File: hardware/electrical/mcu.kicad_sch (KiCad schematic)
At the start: 40 parts, among them J2 TC2030, Q8 2N7002, SW1 TS-1187A-B-A-B, SW2 EVQP7C01K, U8 STM32F446VET6, Y1 24MHz, Y2 32.768kHz

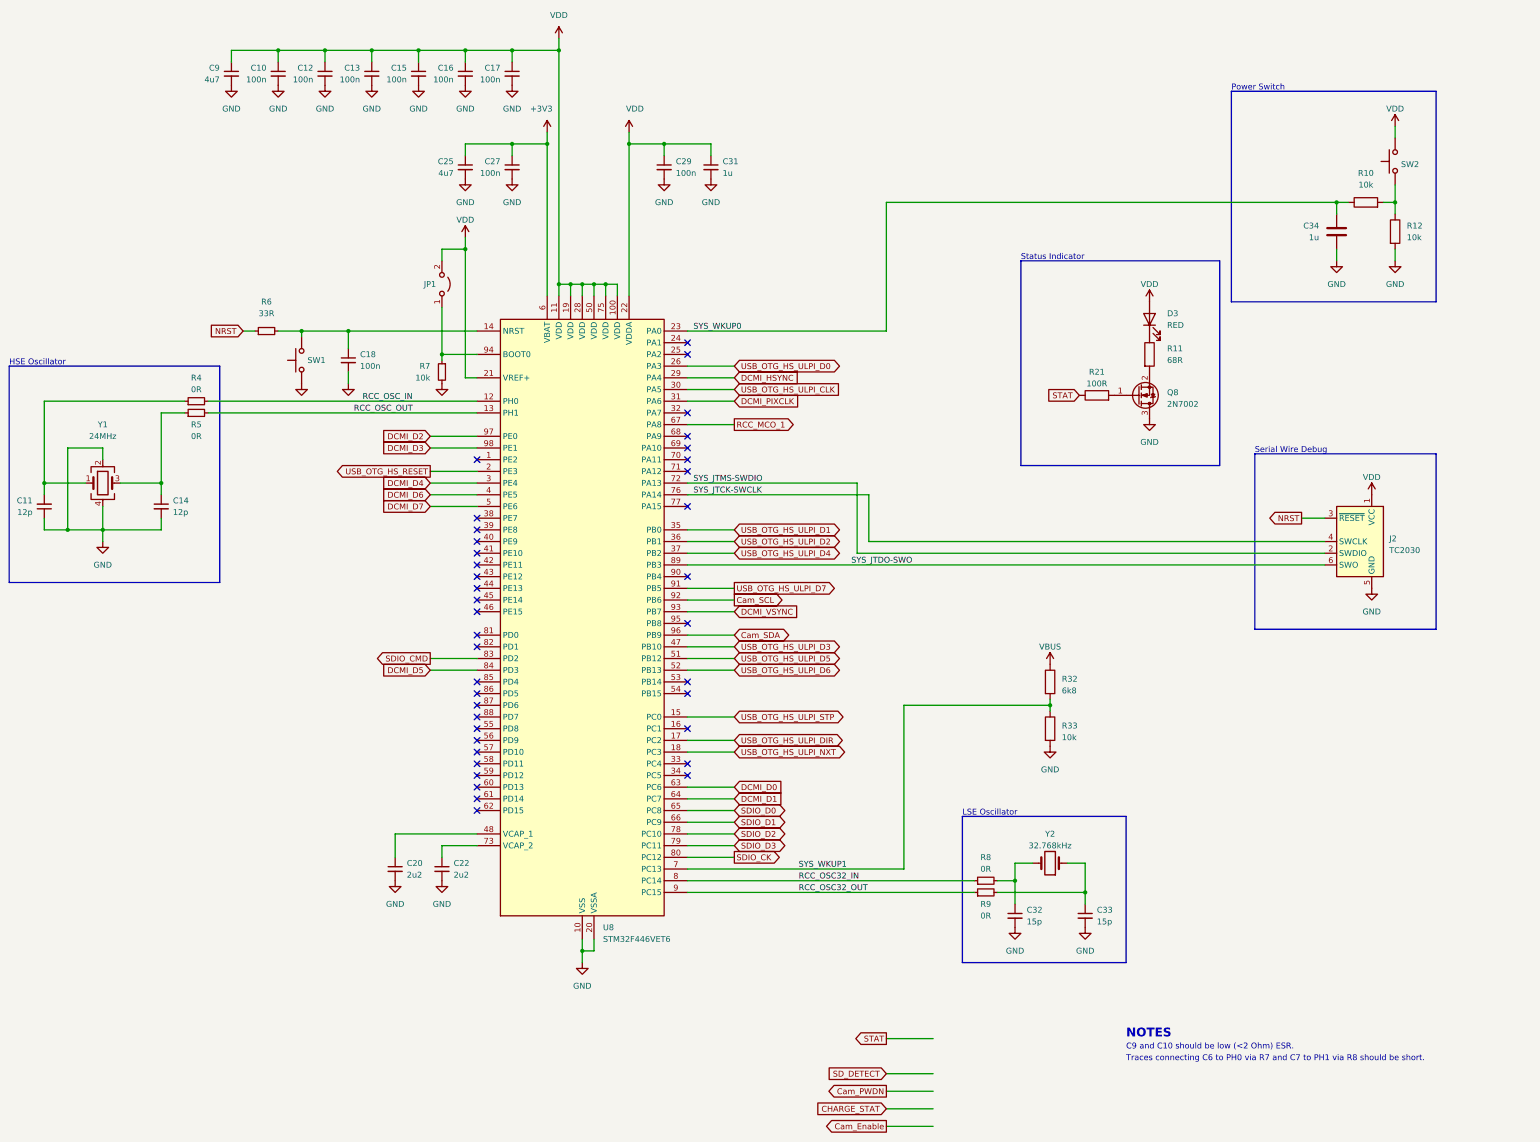
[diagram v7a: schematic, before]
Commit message: Revise power supply
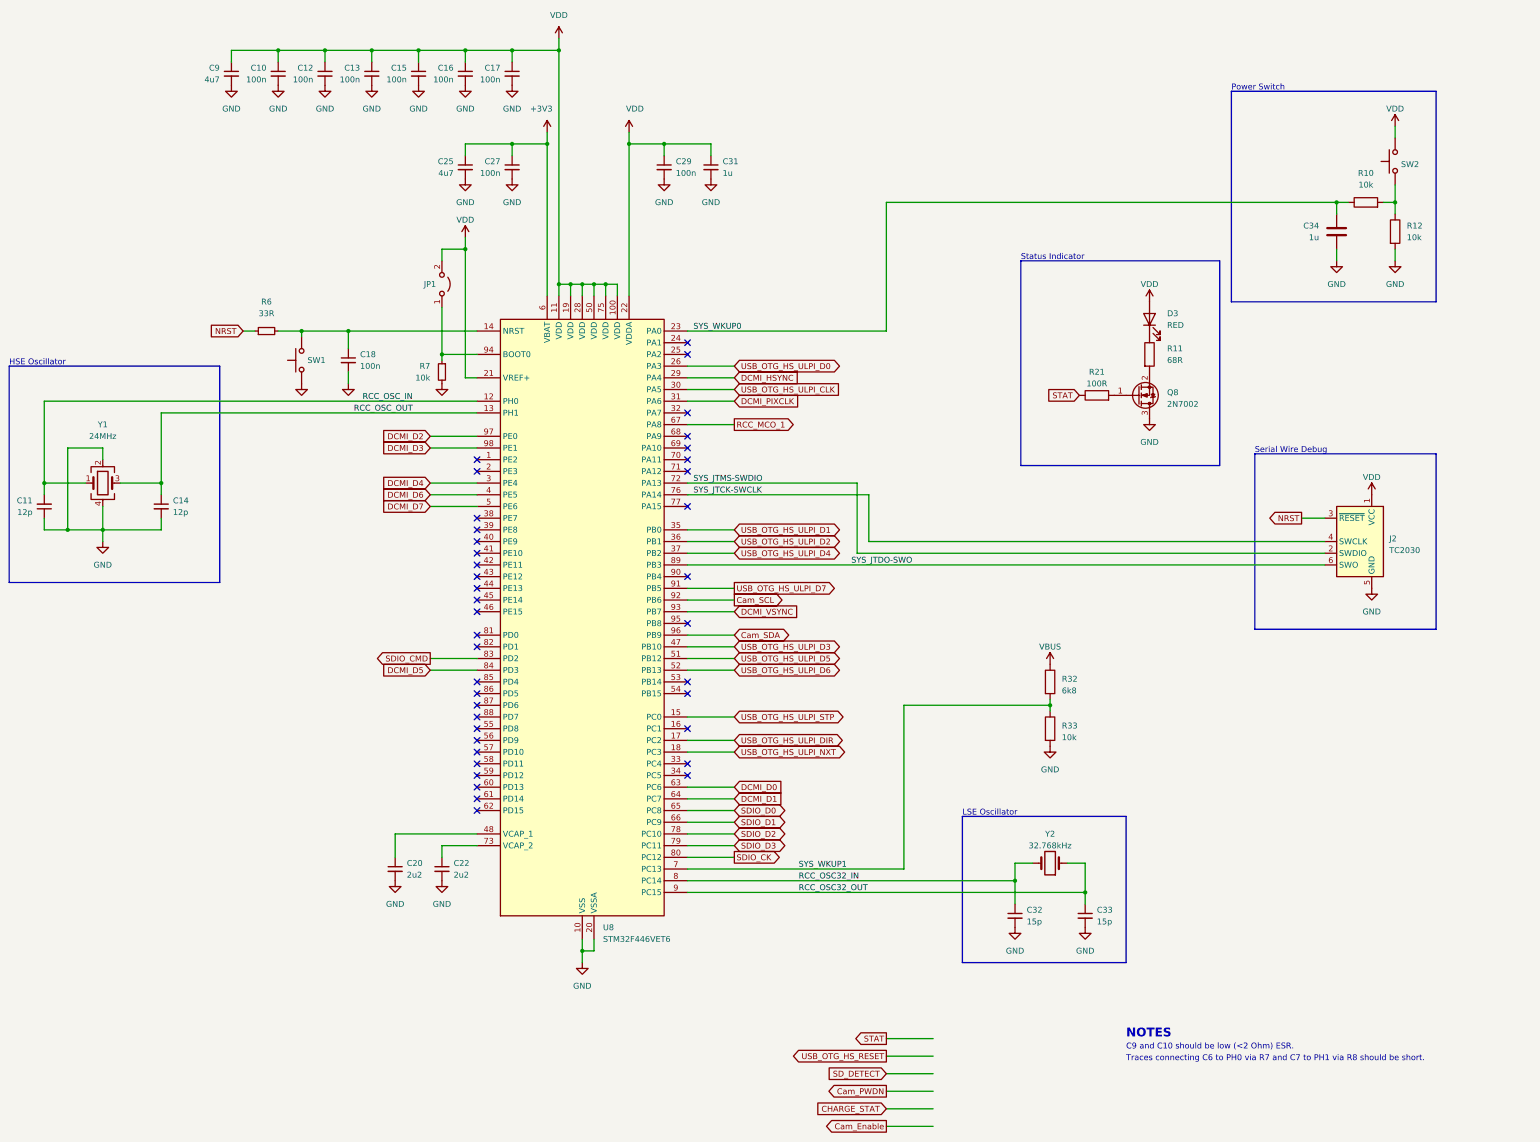
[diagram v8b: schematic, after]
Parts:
- removed R4, R5, R8, R9: 0R, Resistor_SMD:R_0603_1608Metric_Pad0.98x0.95mm_HandSolder, symbol Device:R_Small
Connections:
- net RCC_OSC32_IN: now also C32.1, Y2.2
- net RCC_OSC32_OUT: now also C33.1, Y2.1
- net RCC_OSC_IN: now also C11.2, Y1.1
- net RCC_OSC_OUT: now also C14.1, Y1.3
- net USB_OTG_HS_RESET: no longer U8.2 (PE3)
- no-connect marks 39 -> 40
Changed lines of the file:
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@@
   (no_connect (at 204.47 180.34))
   (no_connect (at 204.47 170.18))
+  (no_connect (at 158.75 124.46))
   (no_connect (at 158.75 182.88))
   (no_connect (at 158.75 121.92))
@@
     (stroke (width 0) (type default))
   )
-  (wire (pts (xy 158.75 124.46) (xy 148.59 124.46))
+  (wire (pts (xy 257.81 251.46) (xy 247.65 251.46))
     (stroke (width 0) (type default))
   )
@@
     (stroke (width 0) (type default))
   )
-  (wire (pts (xy 100.33 111.76) (xy 158.75 111.76))
+  (wire (pts (xy 90.17 111.76) (xy 158.75 111.76))
     (stroke (width 0) (type default))
   )
@@
     (stroke (width 0) (type default))
   )
-  (wire (pts (xy 90.17 111.76) (xy 95.25 111.76))
-    (stroke (width 0) (type default))
-  )
   (wire (pts (xy 135.89 33.02) (xy 135.89 35.56))
     (stroke (width 0) (type default))
@@
     (stroke (width 0) (type default))
   )
-  (wire (pts (xy 204.47 215.9) (xy 266.7 215.9))
-    (stroke (width 0) (type default))
-  )
   (wire (pts (xy 151.13 78.74) (xy 151.13 76.2))
     (stroke (width 0) (type default))
@@
     (stroke (width 0) (type default))
   )
-  (wire (pts (xy 290.83 215.9) (xy 271.78 215.9))
+  (wire (pts (xy 204.47 215.9) (xy 290.83 215.9))
     (stroke (width 0) (type default))
   )
@@
     (stroke (width 0) (type default))
   )
-  (wire (pts (xy 204.47 213.36) (xy 266.7 213.36))
-    (stroke (width 0) (type default))
-  )
   (wire (pts (xy 176.53 83.82) (xy 179.07 83.82))
     (stroke (width 0) (type default))
@@
     (stroke (width 0) (type default))
   )
-  (wire (pts (xy 271.78 213.36) (xy 275.59 213.36))
+  (wire (pts (xy 204.47 213.36) (xy 275.59 213.36))
     (stroke (width 0) (type default))
   )
@@
     (stroke (width 0) (type default))
   )
-  (wire (pts (xy 64.77 109.22) (xy 95.25 109.22))
-    (stroke (width 0) (type default))
-  )
   (wire (pts (xy 186.69 83.82) (xy 186.69 86.36))
     (stroke (width 0) (type default))
@@
     (stroke (width 0) (type default))
   )
-  (wire (pts (xy 100.33 109.22) (xy 158.75 109.22))
+  (wire (pts (xy 64.77 109.22) (xy 158.75 109.22))
     (stroke (width 0) (type default))
   )
@@
     )
   )
-  (global_label "USB_OTG_HS_RESET" (shape output) (at 148.59 124.46 180) (fields_autoplaced)
+  (global_label "USB_OTG_HS_RESET" (shape output) (at 247.65 251.46 180) (fields_autoplaced)
     (effects (font (size 1.27 1.27)) (justify right))
-    (property "Intersheetrefs" "${INTERSHEET_REFS}" (at 127.1182 124.46 0)
+    (property "Intersheetrefs" "${INTERSHEET_REFS}" (at 226.1782 251.46 0)
       (effects (font (size 1.27 1.27)) (justify right) hide)
     )
@@
     )
   )
-  (symbol (lib_id "Device:R_Small") (at 269.24 213.36 90) (unit 1)
-    (in_bom yes) (on_board yes) (dnp no)
-    (property "Reference" "R8" (at 269.24 208.28 90)
-      (effects (font (size 1.27 1.27)))
-    )
-    (property "Value" "0R" (at 269.24 210.82 90)
-      (effects (font (size 1.27 1.27)))
-    )
-    (property "Footprint" "Resistor_SMD:R_0603_1608Metric_Pad0.98x0.95mm_HandSolder" (at 240.03 209.55 0)
-      (effects (font (size 1.27 1.27)) hide)
-    )
-    (property "Datasheet" "https://datasheet.lcsc.com/lcsc/2206010130_UNI-ROYAL-Uniroyal-Elec-0603WAF0000T5E_C21189.pdf" (at 269.24 213.36 0)
-      (effects (font (size 1.27 1.27)) hide)
-    )
-    (property "LCSC Part #" "C21189" (at 269.24 213.36 0)
-      (effects (font (size 1.27 1.27)) hide)
-    )
-    (property "Mfr" "UNI-ROYAL(Uniroyal Elec)" (at 269.24 213.36 0)
-      (effects (font (size 1.27 1.27)) hide)
-    )
-    (property "Mfr. Part #" "0603WAF0000T5E" (at 269.24 213.36 0)
-      (effects (font (size 1.27 1.27)) hide)
-    )
-    (pin "1")
-    (pin "2")
-    (instances
-      (project "3885"
-        (path "/7363a4f0-2da1-4086-abed-ea6709c3a185/239a74a2-fce8-4103-83ba-af4dbf21fb68"
-          (reference "R8") (unit 1)
-        )
-      )
-    )
-  )
   (symbol (lib_id "power:GND") (at 283.21 184.15 0) (unit 1)
     (in_bom yes) (on_board yes) (dnp no) (fields_autoplaced)
@@
     )
   )
-  (symbol (lib_id "Device:R_Small") (at 97.79 109.22 90) (unit 1)
-    (in_bom yes) (on_board yes) (dnp no)
-    (property "Reference" "R4" (at 97.79 104.14 90)
-      (effects (font (size 1.27 1.27)))
-    )
-    (property "Value" "0R" (at 97.79 106.68 90)
-      (effects (font (size 1.27 1.27)))
-    )
-    (property "Footprint" "Resistor_SMD:R_0603_1608Metric_Pad0.98x0.95mm_HandSolder" (at 97.79 109.22 0)
-      (effects (font (size 1.27 1.27)) hide)
-    )
-    (property "Datasheet" "https://datasheet.lcsc.com/lcsc/2206010130_UNI-ROYAL-Uniroyal-Elec-0603WAF0000T5E_C21189.pdf" (at 97.79 109.22 0)
-      (effects (font (size 1.27 1.27)) hide)
-    )
-    (property "LCSC Part #" "C21189" (at 97.79 109.22 0)
-      (effects (font (size 1.27 1.27)) hide)
-    )
-    (property "Mfr" "UNI-ROYAL(Uniroyal Elec)" (at 97.79 109.22 0)
-      (effects (font (size 1.27 1.27)) hide)
-    )
-    (property "Mfr. Part #" "0603WAF0000T5E" (at 97.79 109.22 0)
-      (effects (font (size 1.27 1.27)) hide)
-    )
-    (pin "1")
-    (pin "2")
-    (instances
-      (project "3885"
-        (path "/7363a4f0-2da1-4086-abed-ea6709c3a185/239a74a2-fce8-4103-83ba-af4dbf21fb68"
-          (reference "R4") (unit 1)
-        )
-      )
-    )
-  )
   (symbol (lib_id "Switch:SW_Push") (at 358.14 57.15 90) (unit 1)
     (in_bom yes) (on_board yes) (dnp no) (fields_autoplaced)
@@
         (path "/7363a4f0-2da1-4086-abed-ea6709c3a185/239a74a2-fce8-4103-83ba-af4dbf21fb68"
           (reference "#PWR054") (unit 1)
-        )
-      )
-    )
-  )
-  (symbol (lib_id "Device:R_Small") (at 97.79 111.76 90) (unit 1)
-    (in_bom yes) (on_board yes) (dnp no)
-    (property "Reference" "R5" (at 97.79 114.3 90)
-      (effects (font (size 1.27 1.27)))
-    )
-    (property "Value" "0R" (at 97.79 116.84 90)
-      (effects (font (size 1.27 1.27)))
-    )
-    (property "Footprint" "Resistor_SMD:R_0603_1608Metric_Pad0.98x0.95mm_HandSolder" (at 97.79 111.76 0)
-      (effects (font (size 1.27 1.27)) hide)
-    )
-    (property "Datasheet" "https://datasheet.lcsc.com/lcsc/2206010130_UNI-ROYAL-Uniroyal-Elec-0603WAF0000T5E_C21189.pdf" (at 97.79 111.76 0)
-      (effects (font (size 1.27 1.27)) hide)
-    )
-    (property "LCSC Part #" "C21189" (at 97.79 111.76 0)
-      (effects (font (size 1.27 1.27)) hide)
-    )
-    (property "Mfr" "UNI-ROYAL(Uniroyal Elec)" (at 97.79 111.76 0)
-      (effects (font (size 1.27 1.27)) hide)
-    )
-    (property "Mfr. Part #" "0603WAF0000T5E" (at 97.79 111.76 0)
-      (effects (font (size 1.27 1.27)) hide)
-    )
-    (pin "1")
-    (pin "2")
-    (instances
-      (project "3885"
-        (path "/7363a4f0-2da1-4086-abed-ea6709c3a185/239a74a2-fce8-4103-83ba-af4dbf21fb68"
-          (reference "R5") (unit 1)
         )
       )
@@
         )
       )
-    )
-  )
-  (symbol (lib_id "Device:R_Small") (at 269.24 215.9 90) (unit 1)
-    (in_bom yes) (on_board yes) (dnp no)
-    (property "Reference" "R9" (at 269.24 218.44 90)
-      (effects (font (size 1.27 1.27)))
-    )
-    (property "Value" "0R" (at 269.24 220.98 90)
-      (effects (font (size 1.27 1.27)))
-    )
-    (property "Footprint" "Resistor_SMD:R_0603_1608Metric_Pad0.98x0.95mm_HandSolder" (at 240.03 212.09 0)
-      (effects (font (size 1.27 1.27)) hide)
-    )
-    (property "Datasheet" "https://datasheet.lcsc.com/lcsc/2206010130_UNI-ROYAL-Uniroyal-Elec-0603WAF0000T5E_C21189.pdf" (at 269.24 215.9 0)
-      (effects (font (size 1.27 1.27)) hide)
-    )
-    (property "LCSC Part #" "C21189" (at 269.24 215.9 0)
-      (effects (font (size 1.27 1.27)) hide)
-    )
-    (property "Mfr" "UNI-ROYAL(Uniroyal Elec)" (at 269.24 215.9 0)
-      (effects (font (size 1.27 1.27)) hide)
-    )
-    (property "Mfr. Part #" "0603WAF0000T5E" (at 269.24 215.9 0)
-      (effects (font (size 1.27 1.27)) hide)
-    )
-    (pin "1")
-    (pin "2")
-    (instances
-      (project "3885"
-        (path "/7363a4f0-2da1-4086-abed-ea6709c3a185/239a74a2-fce8-4103-83ba-af4dbf21fb68"
-          (reference "R9") (unit 1)
-        )
-      )
